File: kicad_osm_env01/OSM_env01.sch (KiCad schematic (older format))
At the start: 84 parts, among them J1 Conn_01x12, J2 Conn_01x08, SW1 SW_SPST, SW2 SW_SPST, U3 ESP-WROOM-32

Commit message: schematics awaiting review
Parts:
- removed TP19, TP20, TP21, TP22: Test_Point, symbol Connector:Test_Point
- added J6: Conn_01x06, symbol Connector:Conn_01x06
- added TP19, TP20, TP21, TP22, TP24, TP59, TP60, TP61, TP62, TP63, TP64, TP65, TP66, TP67, TP69, TP70, TP71, TP72, TP73, TP74, TP75, TP76, TP77, TP78: Test_Point, TestPoint:TestPoint_THTPad_D1.0mm_Drill0.5mm, symbol OSM_env01-rescue:Test_Point-Connector-ESP32-EVB_Rev_D-rescue
- R122: value DNF -> 0R
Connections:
- net extra_gpio2 is gone; now on an unnamed net: U3.14 (GPIO12/ADC2_CH5/TOUCH5/RTC_GPIO15/MTDI/HSPIQ/HS2_DATA2/SD_DATA2/EMAC_TXD3)
- net +3V3: now also J6.1 (Pin_1)
- net CS: now also TP62.1
- net ESP_EN: now also J6.6 (Pin_6)
- net ESP_IO0: now also J6.5 (Pin_5)
- net ESP_SCL: now also TP66.1
- net ESP_SDA: now also TP65.1
- net GND: now also J6.2 (Pin_2)
- net HPM_EN: now also TP72.1
- net MIC_LR: now also TP73.1
- net MIC_SCK: now also TP74.1
- net MIC_SD: now also TP78.1
- net MIC_WS: now also TP75.1
- net PULSE_IN1: no longer R24.2
- net RS232_RX: now also J6.3 (Pin_3)
- net RS232_TX: now also J6.4 (Pin_4)
- net STM1_RX: now also TP24.1
- net STM1_TX: now also TP19.1
- net STM2_RX: now also TP76.1
- net STM2_TX: now also TP77.1
- net STM_BOOT0: now also TP71.1
- net STM_MISO: now also TP59.1
- net STM_MOSI: now also TP60.1
- net STM_NRST: now also TP70.1
- net STM_SCK: now also TP61.1
- net STM_SCL: now also TP67.1
- net STM_SDA: now also TP64.1
- net STM_WAKEUP: now also TP69.1
- net extra_gpi3: now also TP20.1
- net extra_gpi4: now also TP21.1
- net extra_gpi5: now also TP22.1
- net extra_gpio1: now also TP63.1
- net MIC_GND: now reaches R122.2
- net STM32L4/PA8: no longer names the net of R122.1
- new net CT_OP: R24.2
- no-connect marks 6 -> 7
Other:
- note added: "CAN Transciever\n"
- note added: "ESP"
- note added: "ESP I2C Pullup"
- note added: "ESP Programming \nheader\n"
- note added: "External Connector"
- note added: "LORA\n"
- note added: "Parts to add:\n-Fiducial\n-Fix particulate in rush issue\n-lora rst not routed and rst through hardware rc"
- note added: "Power Supply and Battery\n"
- note added: "Precision Voltage Reference\n\n"
- note added: "RS485 Transciever\n"
- note added: "STM"
- note added: "STM I2C Pullup"
- note added: "Sensors and IO\n\n"
- note added: "USB Debug\n"
- note removed: "I2C Pullup"
- note removed: "Main Connector"
- note removed: "Parts to add:\n-Fiducial\n-Gpio support\n-add second footprint for lora chip\n-add new microcontroller\n-Fix particulate in rush issue"
- note removed: "add status led"
- moved on the sheet: C1, C12, C13, C18, C19, C20, C21, C27, C28, C29, C30, ESP_STATUS1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

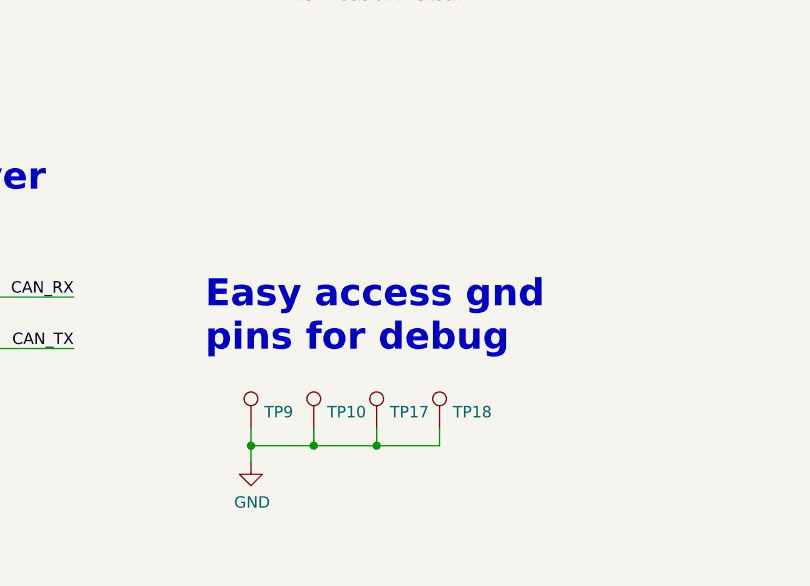
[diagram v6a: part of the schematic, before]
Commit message: updated schematics
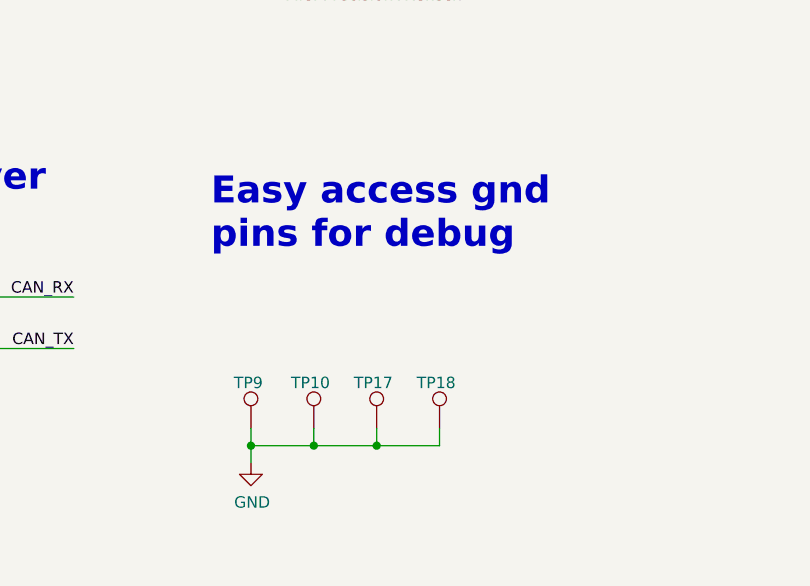
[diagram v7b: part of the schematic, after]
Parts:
- J6: footprint (none) -> Connector_PinHeader_2.54mm:PinHeader_1x06_P2.54mm_Vertical
- TP10, TP17, TP18, TP9: footprint (none) -> TestPoint:TestPoint_THTPad_D1.0mm_Drill0.5mm
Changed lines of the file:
@@
 $Descr A3 16535 11693
 encoding utf-8
-Sheet 1 11
+Sheet 1 12
 Title "Open Smart Monitor"
 Date ""
@@
 U 1 1 608677C1
 P 9275 10000
-F 0 "TP9" H 9333 10072 50  0000 L CNN
+F 0 "TP9" H 9200 10200 50  0000 L CNN
 F 1 "Test_Point" H 9333 10027 50  0001 L CNN
-F 2 "" H 9475 10000 50  0001 C CNN
+F 2 "TestPoint:TestPoint_THTPad_D1.0mm_Drill0.5mm" H 9475 10000 50  0001 C CNN
 F 3 "~" H 9475 10000 50  0001 C CNN
 	1    9275 10000
@@
 U 1 1 6086F915
 P 9550 10000
-F 0 "TP10" H 9608 10072 50  0000 L CNN
+F 0 "TP10" H 9450 10200 50  0000 L CNN
 F 1 "Test_Point" H 9608 10027 50  0001 L CNN
-F 2 "" H 9750 10000 50  0001 C CNN
+F 2 "TestPoint:TestPoint_THTPad_D1.0mm_Drill0.5mm" H 9750 10000 50  0001 C CNN
 F 3 "~" H 9750 10000 50  0001 C CNN
 	1    9550 10000
@@
 U 1 1 608A0166
 P 9825 10000
-F 0 "TP17" H 9883 10072 50  0000 L CNN
+F 0 "TP17" H 9725 10200 50  0000 L CNN
 F 1 "Test_Point" H 9883 10027 50  0001 L CNN
-F 2 "" H 10025 10000 50  0001 C CNN
+F 2 "TestPoint:TestPoint_THTPad_D1.0mm_Drill0.5mm" H 10025 10000 50  0001 C CNN
 F 3 "~" H 10025 10000 50  0001 C CNN
 	1    9825 10000
@@
 U 1 1 608D0934
 P 10100 10000
-F 0 "TP18" H 10158 10072 50  0000 L CNN
+F 0 "TP18" H 10000 10200 50  0000 L CNN
 F 1 "Test_Point" H 10158 10027 50  0001 L CNN
-F 2 "" H 10300 10000 50  0001 C CNN
+F 2 "TestPoint:TestPoint_THTPad_D1.0mm_Drill0.5mm" H 10300 10000 50  0001 C CNN
 F 3 "~" H 10300 10000 50  0001 C CNN
 	1    10100 10000
@@
 F6 "RS485_RX" I R 8125 7475 50
 $EndSheet
-Text Notes 9075 9675 0    118  ~ 24
+Text Notes 9100 9225 0    118  ~ 24
 Easy access gnd\npins for debug\n
 Text Notes 1375 8350 0    79   ~ 0
@@
 F 0 "J6" H 1605 3867 50  0000 L CNN
 F 1 "Conn_01x06" H 1605 3776 50  0000 L CNN
-F 2 "" H 1525 3875 50  0001 C CNN
+F 2 "Connector_PinHeader_2.54mm:PinHeader_1x06_P2.54mm_Vertical" H 1525 3875 50  0001 C CNN
 F 3 "~" H 1525 3875 50  0001 C CNN
 	1    1525 3875

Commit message: started layout
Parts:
- removed J2: Conn_01x08, Connector_JST:JST_EH_B8B-EH-A_1x08_P2.50mm_Vertical, symbol OSM_env01-rescue:Conn_01x08-Connector-ESP32-EVB_Rev_D-rescue
- added J2: Conn_02x10_Counter_Clockwise, Connector_PinHeader_2.00mm:PinHeader_2x10_P2.00mm_Vertical, symbol Connector:Conn_02x10_Counter_Clockwise
- J1: footprint (none) -> Connector_PinHeader_2.54mm:PinHeader_2x06_P2.54mm_Vertical
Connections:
- net +3V3: now also J2.8 (Pin_8)
- net +5V: now also J2.9 (Pin_9)
- net CAN_H: now also J2.16 (Pin_16)
- net CAN_L: now also J2.17 (Pin_17)
- net GND: now also J2.10 (Pin_10), J2.14 (Pin_14), J2.15 (Pin_15), J2.18 (Pin_18), J2.3 (Pin_3), J2.5 (Pin_5), J2.7 (Pin_7)
- net PULSE1_EXT: now also J2.4 (Pin_4)
- net PULSE2_EXT: now also J2.6 (Pin_6)
- net RS485+: now also J2.1 (Pin_1)
- net RS485-: now also J2.2 (Pin_2)
- net CT_OP renamed CT+
- net CT+: now also J2.20 (Pin_20)
- new net CT-: J2.19 (Pin_19)
- no-connect marks 7 -> 10
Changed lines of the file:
@@
 $Descr A3 16535 11693
 encoding utf-8
-Sheet 1 12
+Sheet 1 11
 Title "Open Smart Monitor"
 Date ""
@@
 Text Label 1075 5375 0    50   ~ 0
 5V_IN
-$Comp
-L OSM_env01-rescue:Conn_01x08-Connector-ESP32-EVB_Rev_D-rescue J2
-U 1 1 5E1CC832
-P 5125 9700
-F 0 "J2" H 5205 9692 50  0000 L CNN
-F 1 "Conn_01x08" H 5205 9601 50  0000 L CNN
-F 2 "Connector_JST:JST_EH_B8B-EH-A_1x08_P2.50mm_Vertical" H 5125 9700 50  0001 C CNN
-F 3 "~" H 5125 9700 50  0001 C CNN
-	1    5125 9700
-	1    0    0    -1
-$EndComp
 Text Notes 3725 9000 0    118  ~ 24
 External Connector
@@
 L OSM_env01-rescue:GND-ESP32-EVB_Rev_D #PWR07
 U 1 1 5EEBB9FF
-P 4825 10175
-F 0 "#PWR07" H 4825 9925 50  0001 C CNN
-F 1 "GND" H 4830 10002 50  0000 C CNN
-F 2 "" H 4825 10175 60  0000 C CNN
-F 3 "" H 4825 10175 60  0000 C CNN
-	1    4825 10175
-	1    0    0    -1
-$EndComp
-Wire Wire Line
-	4825 10175 4825 10000
+P 4825 10425
+F 0 "#PWR07" H 4825 10175 50  0001 C CNN
+F 1 "GND" H 4830 10252 50  0000 C CNN
+F 2 "" H 4825 10425 60  0000 C CNN
+F 3 "" H 4825 10425 60  0000 C CNN
+	1    4825 10425
+	1    0    0    -1
+$EndComp
+Wire Wire Line
+	4825 10425 4825 10300
 Wire Wire Line
 	4825 9600 4925 9600
@@
 F 0 "J1" H 2280 9892 50  0000 L CNN
 F 1 "Conn_01x12" H 2280 9801 50  0000 L CNN
-F 2 "" H 2200 9900 50  0001 C CNN
+F 2 "Connector_PinHeader_2.54mm:PinHeader_2x06_P2.54mm_Vertical" H 2200 9900 50  0001 C CNN
 F 3 "~" H 2200 9900 50  0001 C CNN
 	1    2200 9900
@@
 extra_gpio1
 Wire Wire Line
-	4925 10100 4925 10200
-Wire Wire Line
-	4925 10200 5000 10200
-Wire Wire Line
-	5000 10200 5000 10300
-Wire Wire Line
-	5000 10300 5475 10300
-Wire Wire Line
-	5475 10300 5475 10200
+	4425 10350 4425 10250
 $Comp
 L power:+3V3 #PWR011
 U 1 1 61210753
-P 5475 10200
-F 0 "#PWR011" H 5475 10050 50  0001 C CNN
-F 1 "+3V3" H 5490 10373 50  0000 C CNN
-F 2 "" H 5475 10200 50  0001 C CNN
-F 3 "" H 5475 10200 50  0001 C CNN
-	1    5475 10200
+P 4425 10250
+F 0 "#PWR011" H 4425 10100 50  0001 C CNN
+F 1 "+3V3" H 4440 10423 50  0000 C CNN
+F 2 "" H 4425 10250 50  0001 C CNN
+F 3 "" H 4425 10250 50  0001 C CNN
+	1    4425 10250
 	1    0    0    -1
 $EndComp
@@
 F13 "MIC_GND" I R 14900 5775 50
 F14 "CT+" I R 14900 6475 50
+F15 "CT-" I R 14900 6625 50
 $EndSheet
 Text Label 7275 3575 2    50   ~ 0
@@
 	14900 6475 15200 6475
 Text Label 15200 6475 2    50   ~ 0
-CT_OP
-Text Label 14875 1500 2    50   ~ 0
-CT_OP
+CT+
 Text Notes 9550 3325 0    118  ~ 24
 ESP
@@
 Text Notes 9175 7300 0    118  ~ 24
 Precision Voltage Reference\n\n
+Text Label 5750 9500 2    50   ~ 0
+CT-
+Wire Wire Line
+	5750 9500 5425 9500
+Text Label 5750 9400 2    50   ~ 0
+CT+
+Wire Wire Line
+	5750 9400 5425 9400
+$Comp
+L OSM_env01:GND #PWR?
+U 1 1 60812B47
+P 5625 10425
+AR Path="/611AF79D/60812B47" Ref="#PWR?"  Part="1"
+AR Path="/608F4675/60812B47" Ref="#PWR?"  Part="1"
+AR Path="/60812B47" Ref="#PWR0142"  Part="1"
+F 0 "#PWR0142" H 5625 10175 50  0001 C CNN
+F 1 "GND" H 5630 10252 50  0000 C CNN
+F 2 "" H 5625 10425 60  0000 C CNN
+F 3 "" H 5625 10425 60  0000 C CNN
+	1    5625 10425
+	1    0    0    -1
+$EndComp
+Wire Wire Line
+	5425 9600 5625 9600
+Wire Wire Line
+	5625 9600 5625 9900
+Wire Wire Line
+	14900 6625 15200 6625
+Text Label 15200 6625 2    50   ~ 0
+CT-
+Text Label 14875 1500 2    50   ~ 0
+CT+
+$Comp
+L Connector:Conn_02x10_Counter_Clockwise J2
+U 1 1 6088193B
+P 5125 9800
+F 0 "J2" H 5175 10417 50  0000 C CNN
+F 1 "Conn_02x10_Counter_Clockwise" H 5175 10326 50  0000 C CNN
+F 2 "Connector_PinHeader_2.00mm:PinHeader_2x10_P2.00mm_Vertical" H 5125 9800 50  0001 C CNN
+F 3 "~" H 5125 9800 50  0001 C CNN
+	1    5125 9800
+	1    0    0    -1
+$EndComp
+$Comp
+L power:+5V #PWR0143
+U 1 1 6091E75E
+P 4175 10250
+F 0 "#PWR0143" H 4175 10100 50  0001 C CNN
+F 1 "+5V" H 4190 10423 50  0000 C CNN
+F 2 "" H 4175 10250 50  0001 C CNN
+F 3 "" H 4175 10250 50  0001 C CNN
+	1    4175 10250
+	1    0    0    -1
+$EndComp
+Wire Wire Line
+	4425 10350 4625 10350
+Wire Wire Line
+	4625 10350 4625 10100
+Wire Wire Line
+	4925 10100 4625 10100
+Wire Wire Line
+	4175 10400 4700 10400
+Wire Wire Line
+	4700 10400 4700 10200
+Wire Wire Line
+	4700 10200 4925 10200
+Wire Wire Line
+	4175 10250 4175 10400
+Wire Wire Line
+	4825 10300 4925 10300
+Connection ~ 4825 10300
+Wire Wire Line
+	4825 10300 4825 10000
+Wire Wire Line
+	5425 9700 5825 9700
+Text Label 5825 9700 2    50   ~ 0
+CAN_L
+Wire Wire Line
+	5425 9800 5825 9800
+Text Label 5825 9800 2    50   ~ 0
+CAN_H
+Wire Wire Line
+	5425 9900 5625 9900
+Connection ~ 5625 9900
+Wire Wire Line
+	5625 9900 5625 10000
+Wire Wire Line
+	5425 10000 5625 10000
+Connection ~ 5625 10000
+Wire Wire Line
+	5625 10000 5625 10425
+NoConn ~ 5425 10100
+NoConn ~ 5425 10200
+NoConn ~ 5425 10300
 $EndSCHEMATC
